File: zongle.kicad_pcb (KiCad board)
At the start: 2 copper layers, 8.2 x 9.8 mm, 5 parts, among them J1 USB_C_Receptacle_USB2.0_14P, J2 TC2030_SWD, U1 453-00059R, U2 TPD2EUSB30

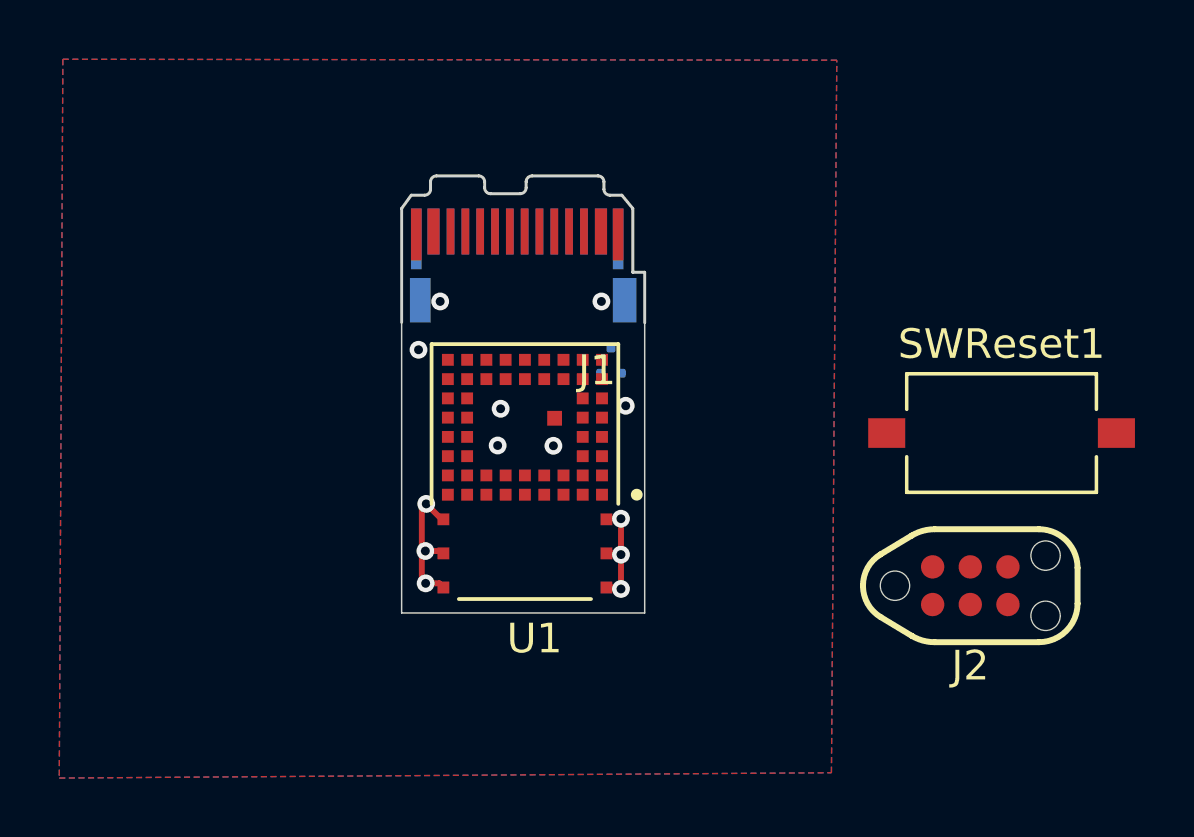
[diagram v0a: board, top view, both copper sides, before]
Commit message: further routing. still missig footprints for testpoints and reset button, most of the routing is now done, will need some cleanup + drc fixesw
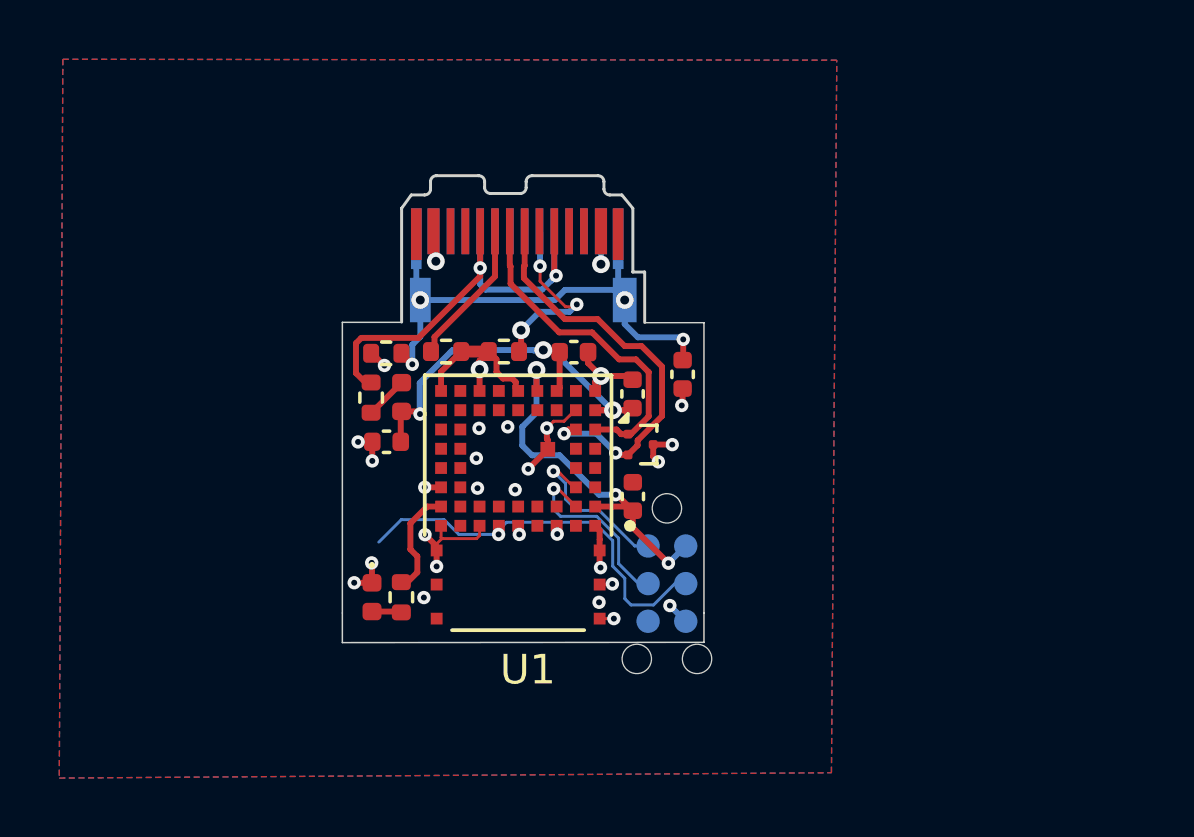
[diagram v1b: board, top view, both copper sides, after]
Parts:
- removed J1: USB_C_Receptacle_USB2.0_14P, Connector_USB:USB_C_Plug_JAE_DX07P024AJ1
- removed J2: TC2030_SWD, marbastlib-various:CON_TC2030_outlined
- removed SWReset1: SW_Push, Button_Switch_SMD:SW_Tactile_SPST_NO_Straight_CK_PTS636Sx25SMTRLFS
- removed U2: TPD2EUSB30, Package_TO_SOT_SMD:Texas_DRT-3
- added C11: 4.7uF, Capacitor_SMD:C_0402_1005Metric, F.Cu at (155.6, 110.1)
- added C22: 10uF, Capacitor_SMD:C_0402_1005Metric, F.Cu at (147.3, 111.7)
- added C23: 100nF, Capacitor_SMD:C_0402_1005Metric, F.Cu at (153.6, 108.7)
- added C24: 100nF, Capacitor_SMD:C_0402_1005Metric, F.Cu at (155.6, 113.5)
- added C25: 1nF, Capacitor_SMD:C_0402_1005Metric, F.Cu at (157.3, 109.4)
- added ESD1: TPD2EUSB30, Package_TO_SOT_SMD:Texas_DRT-3, F.Cu at (155.8, 111.8)
- added F1: 750mA, Fuse:Fuse_0402_1005Metric, F.Cu at (147.8, 110.2)
- added FB1: 100 Ω @ 100 MHz, Resistor_SMD:R_0402_1005Metric, F.Cu at (146.8, 110.2)
- added LED_STATUS1: LED, LED_SMD:LED_0402_1005Metric, F.Cu at (146.8, 116.9)
- added R11: 5k1, Resistor_SMD:R_0402_1005Metric, F.Cu at (149.3, 108.6)
- added R12: 5k1, Resistor_SMD:R_0402_1005Metric, F.Cu at (151.2, 108.6)
- added R21: 3.3k, Resistor_SMD:R_0402_1005Metric, F.Cu at (147.8, 116.9)
- added R24: 1M, Resistor_SMD:R_0402_1005Metric, F.Cu at (147.3, 108.7)
- added SWD1: TC2030_SWD, marbastlib-various:CON_TC2030_outlined, B.Cu at (156.7, 116.5)
- added USB_C1: USB_C_Receptacle_USB2.0_14P, Connector_USB:USB_C_Plug_JAE_DX07P024AJ1, F.Cu at (151.7, 105.7)
- moved U1 1.07 mm to (151.7, 113.7)
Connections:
- U1 pad 10: unconnected-(U1-SIO_03/AIN1-Pad10) -> LED_ST
- U1 pad 21: unconnected-(U1-VDD_NRF-Pad21) -> VDD_NRF
- U1 pad 30: unconnected-(U1-VDD_NRF_1-Pad30) -> VDD_NRF
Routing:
- net GND: track 8.79 -> 27.6 mm, vias 11 -> 30
- net Net-(USB_C1-SHIELD): track 0.00 -> 18.0 mm, vias 0 -> 4
- net Net-(FB1-Pad1): track 0.00 -> 16.4 mm, vias 0 -> 2
- net +5V: track 0.00 -> 16.0 mm, vias 0 -> 3
- net D-: track 0.00 -> 13.9 mm, vias 0 -> 2
- net RST: track 0.00 -> 13.8 mm, vias 0 -> 1
- net VDD_NRF: track 0.00 -> 12.6 mm, vias 0 -> 3
- net D+: track 0.00 -> 11.3 mm
- net Net-(USB_C1-CC2): track 0.00 -> 6.46 mm, vias 0 -> 3
- net SWCLK: track 0.00 -> 6.42 mm, vias 0 -> 1
- net SWDIO: track 0.00 -> 5.67 mm, vias 0 -> 1
- net Net-(USB_C1-CC1): track 0.00 -> 4.95 mm
- net LED_ST: track 0.00 -> 3.70 mm
- net Net-(F1-Pad1): track 0.00 -> 1.54 mm
- net Net-(LED_STATUS1-A): track 0.00 -> 1.00 mm
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- added copper zone on In1.Cu, net GND
- added copper zone on In2.Cu, net GND
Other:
- board size 8.2 x 9.8 mm -> 12.2 x 10.8 mm
- copper layers 2 -> 4

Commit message: used actual symbol of usb c port. redid routing. saved 2mm in length. fixed 3d model for usb c receptacle, now using 6 layers for cheap via in pad to avoid having to pay for microvias
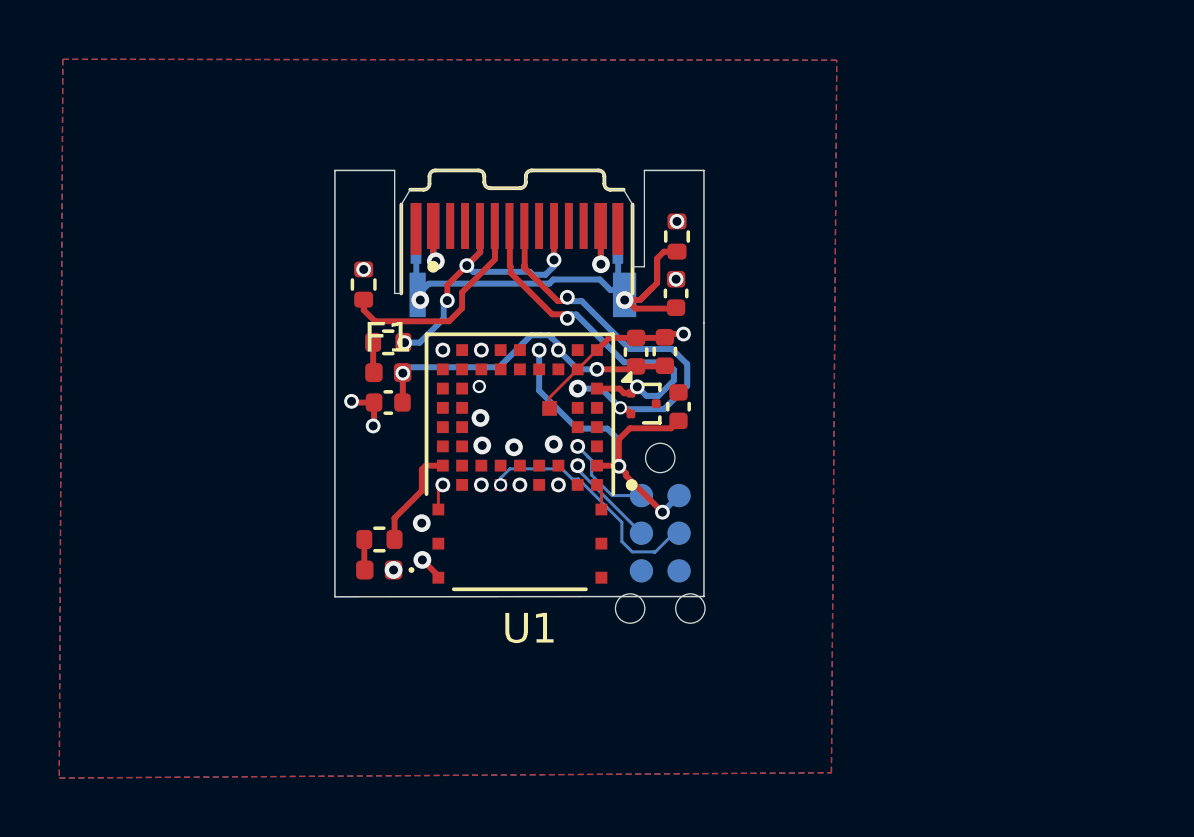
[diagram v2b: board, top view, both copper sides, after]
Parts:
- removed C25: 1nF, Capacitor_SMD:C_0402_1005Metric
- removed R11, R12: 5k1, Resistor_SMD:R_0402_1005Metric
- removed R24: 1M, Resistor_SMD:R_0402_1005Metric
- removed USB_C1: USB_C_Receptacle_USB2.0_14P, Connector_USB:USB_C_Plug_JAE_DX07P024AJ1
- added C26: 1nF, Capacitor_SMD:C_0402_1005Metric, F.Cu at (157.0, 106.7)
- added R23: 5k1, Resistor_SMD:R_0402_1005Metric, F.Cu at (146.5, 106.4)
- added R26: 1M, Resistor_SMD:R_0402_1005Metric, F.Cu at (157.1, 104.8)
- added USB_C2: DX07P024AJ1R1500, USB_C_MALE_LONG:USB_C_MALE_LONG, F.Cu at (151.7, 102.5)
- moved C24 3.40 mm to (157.1, 110.5)
- moved C23 2.10 mm to (155.7, 108.7), turned to 90 degrees
- moved R21 2.09 mm to (147.0, 115.0), turned to 180 degrees
- moved FB1 1.95 mm to (147.3, 108.3), turned to 180 degrees
- moved C11 1.80 mm to (156.7, 108.6)
- moved SWD1 1.71 mm to (156.5, 114.8)
- moved ESD1 1.38 mm to (155.9, 110.4)
- moved U1 1.38 mm to (151.8, 112.3)
- moved C22 1.33 mm to (147.3, 110.3)
- moved LED_STATUS1 0.95 mm to (147.0, 116.0), turned to 180 degrees
- moved F1 0.94 mm to (147.3, 109.3), turned to 0 degrees
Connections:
- FB1 pad 1: Net-(FB1-Pad1) -> VBUS_Raw
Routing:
- net Net-(C26-Pad1): track 0.00 -> 18.4 mm, vias 0 -> 2
- net Net-(USB_C1-SHIELD): track 18.0 -> 0.00 mm, vias 4 -> 0
- net Net-(FB1-Pad1): track 16.4 -> 0.00 mm, vias 2 -> 0
- net GND: track 27.6 -> 14.9 mm, vias 30 -> 22
- net VBUS_Raw: track 0.00 -> 11.1 mm, vias 0 -> 4
- net Net-(USB_C2-CC): track 0.00 -> 7.07 mm
- net Net-(USB_C1-CC2): track 6.46 -> 0.00 mm, vias 3 -> 0
- net RST: track 13.8 -> 8.20 mm
- net Net-(USB_C1-CC1): track 4.95 -> 0.00 mm
- net +5V: track 16.0 -> 11.0 mm
- net SWCLK: track 6.42 -> 3.17 mm
- net SWDIO: track 5.67 -> 3.19 mm
- net D+: track 11.3 -> 11.8 mm, vias 0 -> 2
- net Net-(F1-Pad1): track 1.54 -> 1.03 mm
- net D-: track 13.9 -> 13.7 mm, vias 2 -> 3
- added copper zone on In3.Cu, net GND
- added copper zone on In4.Cu, net GND
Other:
- board size 12.2 x 10.8 mm -> 12.4 x 14.4 mm
- copper layers 4 -> 6

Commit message: some layout changes. fixed testpoint size. found fitting reset button. moved all parts to the top side, now missing part asignment
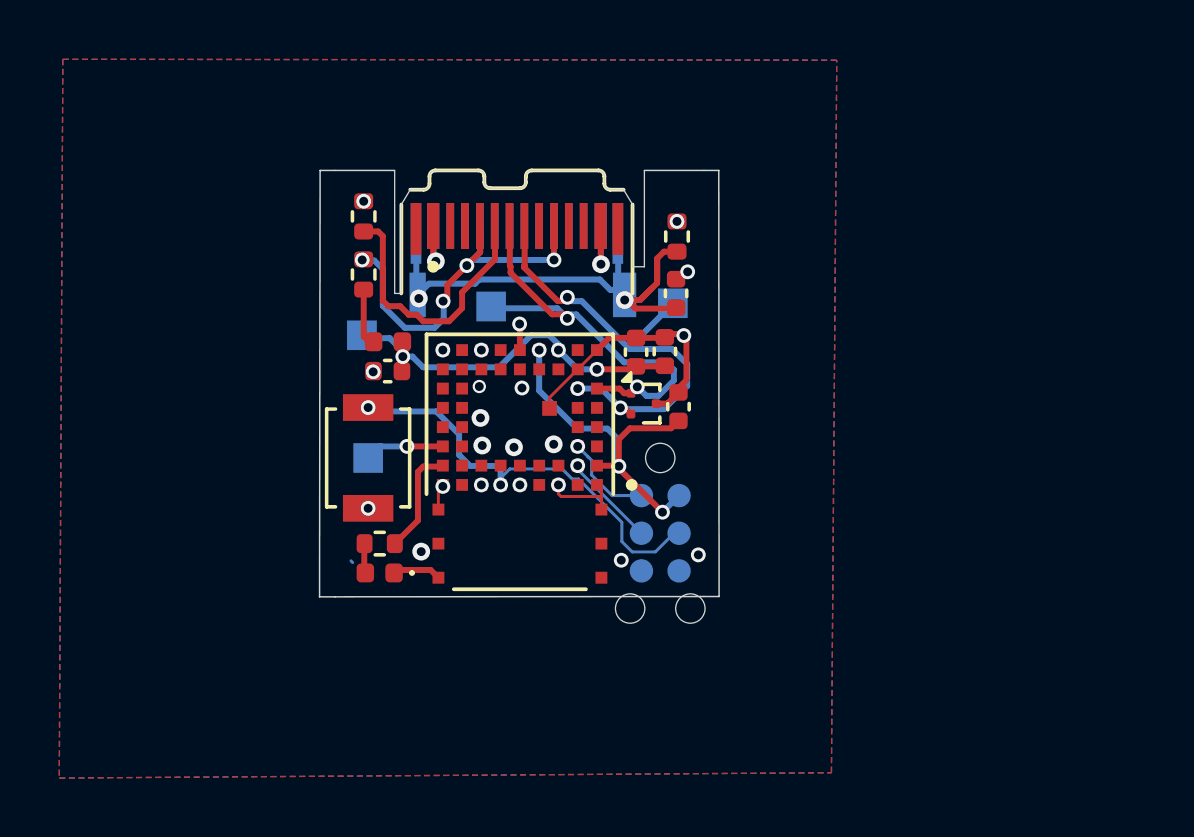
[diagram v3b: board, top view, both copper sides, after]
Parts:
- added SWReset_1: B3U-1100P, Button_Switch_SMD:SW_SPST_B3U-1000P, F.Cu at (146.7, 112.2)
- added Tp+5v: TestPoint, TestPoint:TestPoint_Pad_1.0x1.0mm, B.Cu at (146.4, 108.1)
- added TpD+: TestPoint, TestPoint:TestPoint_Pad_1.0x1.0mm, B.Cu at (150.8, 107.1)
- added TpD-: TestPoint, TestPoint:TestPoint_Pad_1.0x1.0mm, B.Cu at (156.9, 107.0)
- added TpGND: TestPoint, TestPoint:TestPoint_Pad_1.0x1.0mm, B.Cu at (146.7, 112.2)
- moved FB1 2.44 mm to (146.5, 106.0), turned to -90 degrees
- moved R23 2.30 mm to (146.5, 104.1)
- moved C22 1.06 mm to (147.3, 109.3)
- moved F1 1.04 mm to (147.3, 108.3)
- moved R21 0.14 mm to (147.0, 115.1)
- moved LED_STATUS1 0.10 mm to (147.0, 116.1)
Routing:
- net GND: track 14.9 -> 23.3 mm, vias 22 -> 25
- net RST: track 8.20 -> 14.4 mm, vias 1 -> 2
- net VBUS_Raw: track 11.1 -> 14.8 mm
- net D+: track 11.8 -> 14.4 mm
- net Net-(USB_C2-CC): track 7.07 -> 9.09 mm
- net D-: track 13.7 -> 15.5 mm
- net +5V: track 11.0 -> 12.4 mm
- net Net-(F1-Pad1): track 1.03 -> 2.06 mm
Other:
- board size 12.4 x 14.4 mm -> 13.5 x 14.4 mm

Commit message: some routing cleanup, some drc fixes, assigned parts to every footprint
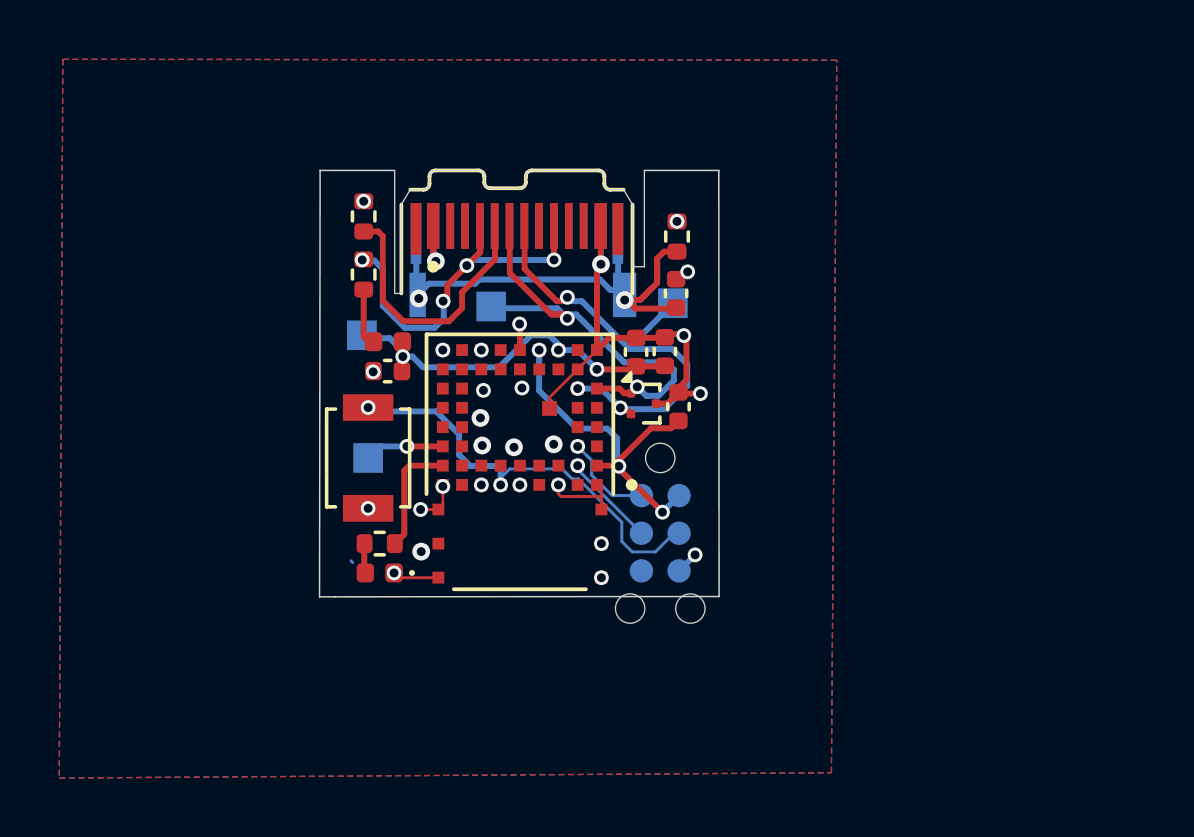
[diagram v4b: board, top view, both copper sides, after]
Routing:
- net GND: track 23.3 -> 28.4 mm, vias 25 -> 29
- net D+: track 14.4 -> 15.0 mm

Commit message: minor changes to the routing. final tweaks for first version
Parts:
- moved C24 3.53 mm to (155.8, 113.7), turned to 90 degrees
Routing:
- net GND: track 28.4 -> 33.2 mm, vias 29 -> 31
- net VDD_NRF: track 12.5 -> 9.75 mm

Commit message: added version indicator on pcb
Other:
- board text added: "zongle@0.0.1"

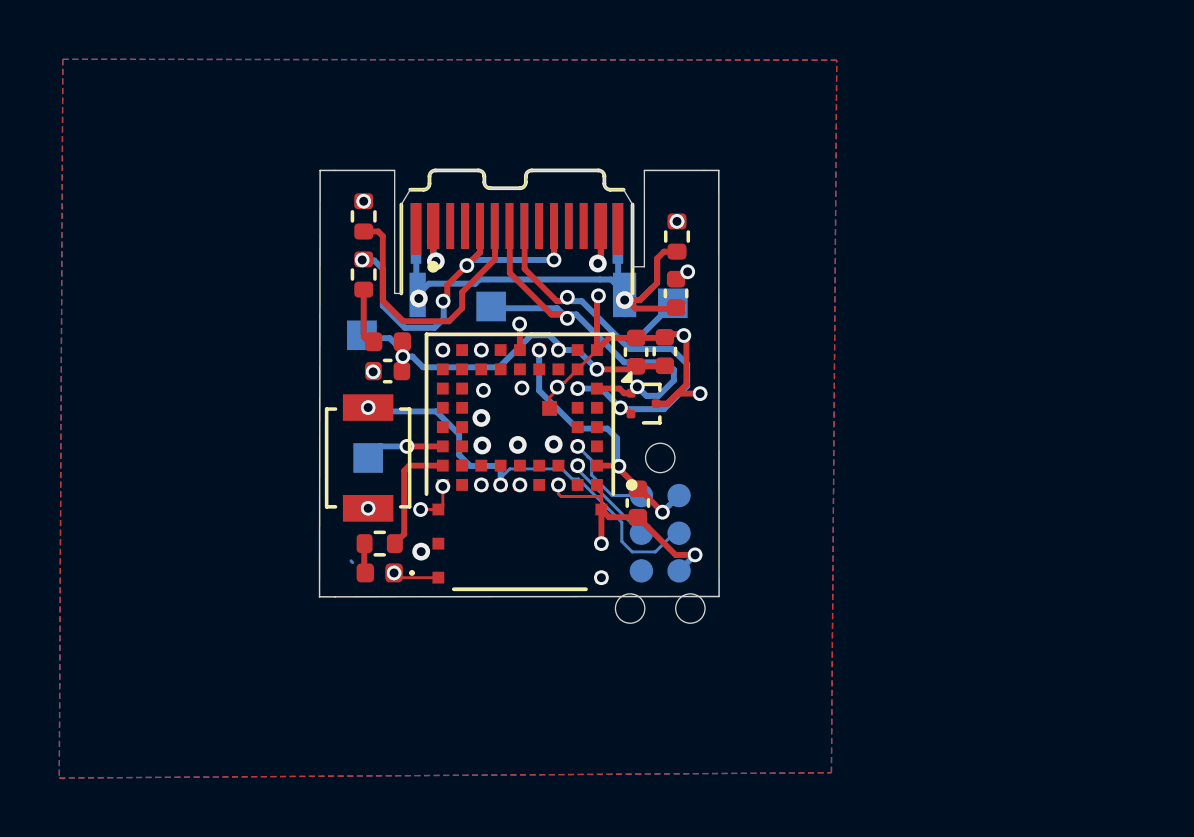
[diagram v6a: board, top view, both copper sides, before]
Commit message: moved some components furhter from the antenna, modified usb testpoints to be smaller and not interfere with the signal (hopefully :o ), changed track width to 0.2mm on most components to avoid production issues
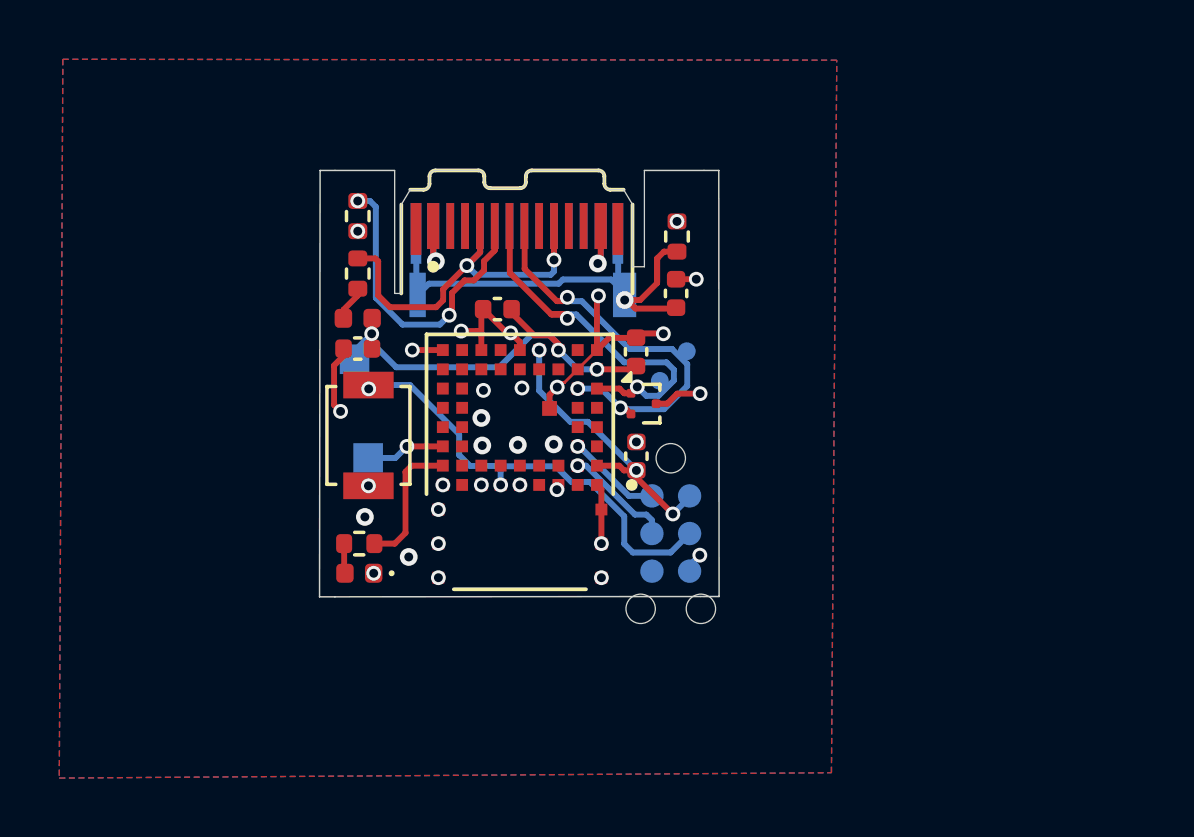
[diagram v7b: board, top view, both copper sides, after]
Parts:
- moved TpD+ 6.22 mm to (156.5, 109.6)
- moved C23 4.90 mm to (151.0, 107.2), turned to 180 degrees
- moved TpD- 1.69 mm to (157.4, 108.6)
- moved C24 1.58 mm to (155.7, 112.2), turned to -90 degrees
- moved F1 1.29 mm to (146.3, 107.5)
- moved C22 1.26 mm to (146.3, 108.5)
- moved C11 0.97 mm to (155.7, 108.6)
- moved Tp+5v 0.85 mm to (146.2, 108.9)
- moved SWReset_1 0.76 mm to (146.7, 111.5)
- moved R21 0.69 mm to (146.3, 115.1)
- moved LED_STATUS1 0.69 mm to (146.4, 116.1)
- moved SWD1 0.36 mm to (156.9, 114.8)
- moved FB1 0.20 mm to (146.3, 106.0)
- moved R23 0.20 mm to (146.3, 104.1), turned to 90 degrees
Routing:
- net GND: track 33.2 -> 27.3 mm, vias 31 -> 35
- net D+: track 15.0 -> 12.4 mm
- net +5V: track 12.4 -> 14.6 mm
- net D-: track 15.9 -> 14.1 mm
- net Net-(C26-Pad1): track 18.3 -> 16.7 mm, vias 2 -> 1
- net Net-(USB_C2-CC): track 9.09 -> 10.6 mm, vias 0 -> 2
- net RST: track 14.4 -> 15.3 mm
- net Net-(F1-Pad1): track 2.06 -> 1.22 mm
- net LED_ST: track 3.96 -> 4.61 mm
- net SWCLK: track 3.17 -> 3.72 mm
- net VBUS_Raw: track 14.8 -> 14.3 mm, vias 4 -> 2
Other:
- board text added: "zongle@0.0.2"
- board text removed: "zongle@0.0.1"
